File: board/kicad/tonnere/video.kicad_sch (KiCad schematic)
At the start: 38 parts, among them J4 DE15_Pins_HighDensity_Mountin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, J5 HDMI_A, U1 TPD4E02B04DQA, U12 TPD4E02B04DQA, U2 TPD4E02B04DQA, U25 THS7316DR, U3 TPD4E02B04DQA

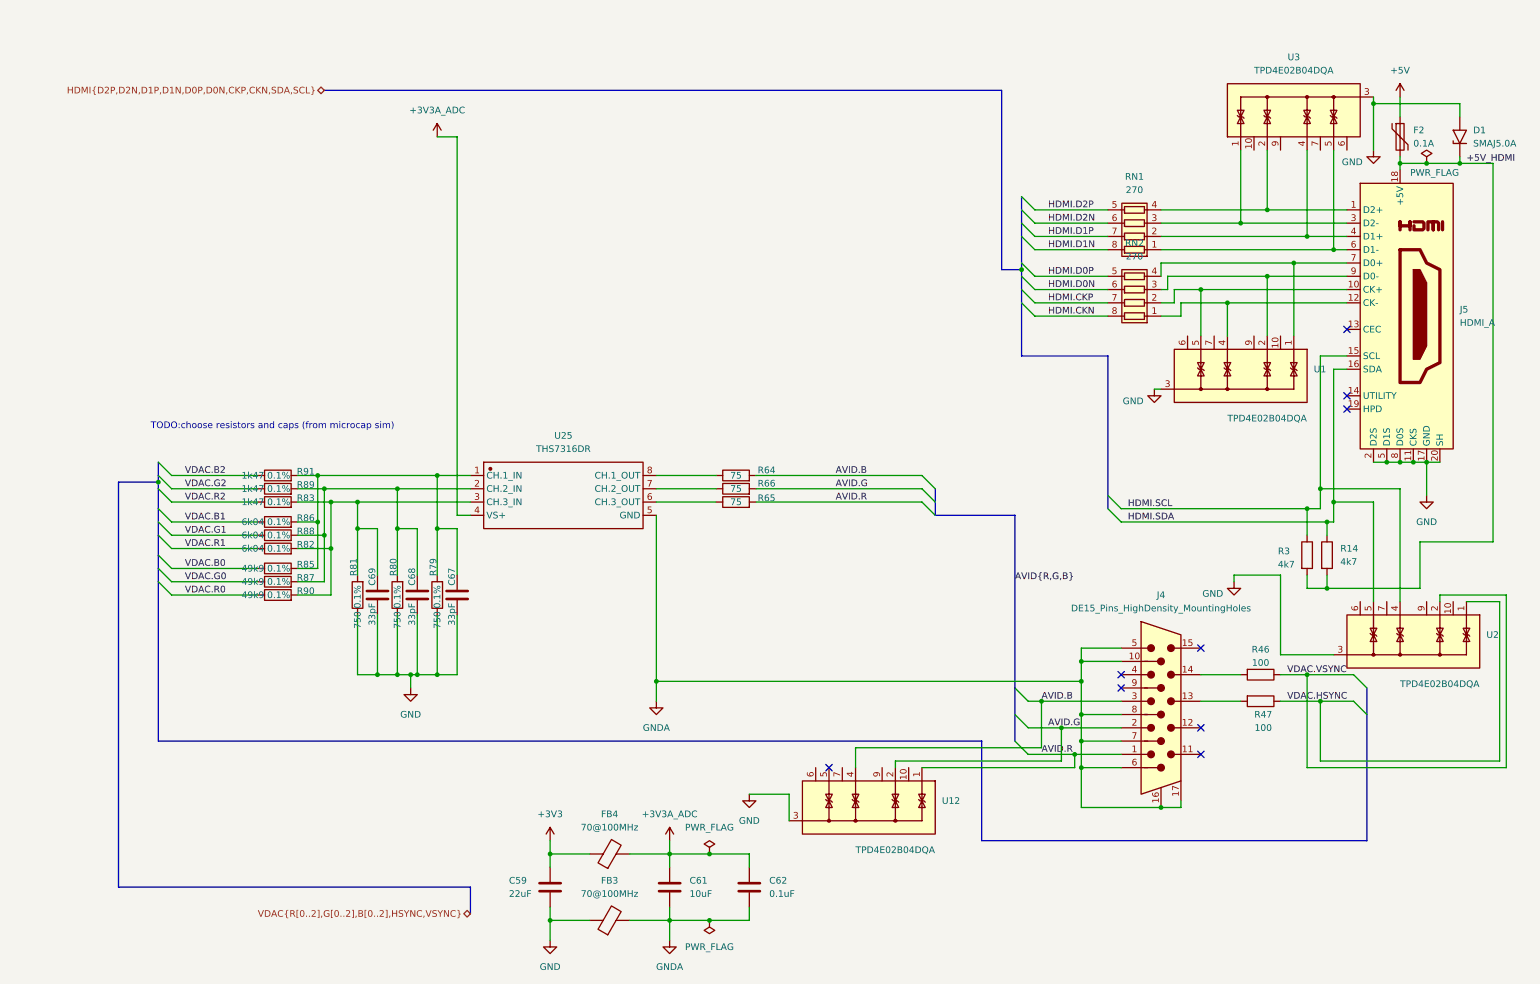
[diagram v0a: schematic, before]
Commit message: Changed video dac to 5 bit R2R and 6th-8th bits as pattern and/or sigma delta.
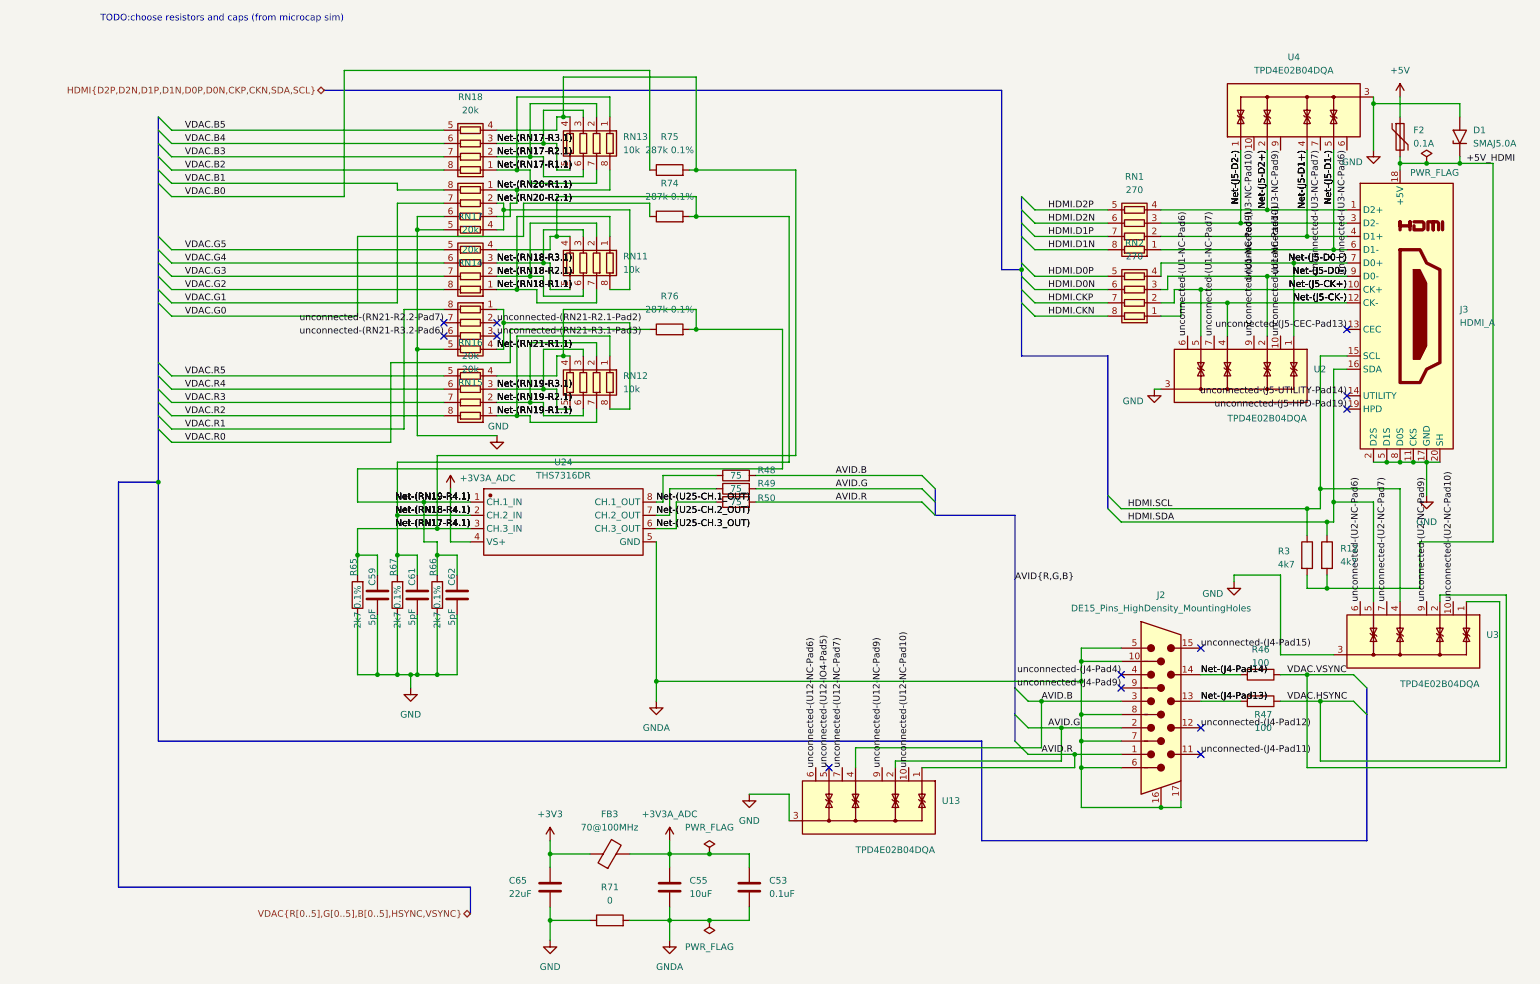
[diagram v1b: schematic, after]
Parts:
- removed FB3: 70@100MHz, Inductor_SMD:L_0805_2012Metric, symbol Device:FerriteBead
- removed R82, R86, R88: 6k04 0.1%, Resistor_SMD:R_0603_1608Metric, symbol Device:R
- removed R83, R89, R91: 1k47 0.1%, Resistor_SMD:R_0603_1608Metric, symbol Device:R
- removed R85, R87, R90: 49k9 0.1%, Resistor_SMD:R_0603_1608Metric, symbol Device:R
- added R71: 0, Resistor_SMD:R_0805_2012Metric, symbol Device:R
- added R74, R75, R76: 287k 0.1%, Resistor_SMD:R_0603_1608Metric, symbol Device:R
- added RN11, RN12, RN13: 10k, Resistor_SMD:R_Array_Convex_4x0402, symbol Device:R_Pack04
- added RN14, RN15, RN16, RN17, RN18: 20k, Resistor_SMD:R_Array_Convex_4x0402, symbol Device:R_Pack04
- C59: renamed from C69; value 33pF -> 5pF; LCSC C1663 -> C282071
- C61: renamed from C68; value 33pF -> 5pF; LCSC C1663 -> C282071
- C62: renamed from C67; value 33pF -> 5pF; LCSC C1663 -> C282071
- R65: renamed from R81; value 750 0.1% -> 2k7 0.1%; LCSC C543637 -> C705760
- R66: renamed from R79; value 750 0.1% -> 2k7 0.1%; LCSC C543637 -> C705760
- R67: renamed from R80; value 750 0.1% -> 2k7 0.1%; LCSC C543637 -> C705760
- renumbered C62 to C53, C61 to C55, C59 to C65, FB4 to FB3, J4 to J2, J5 to J3, R14 to R12, R64 to R48, R66 to R49, R65 to R50, U12 to U13, U1 to U2, U25 to U24, U2 to U3, U3 to U4
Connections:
- net GND: now also R71.1, RN14.5 (R4.2), RN14.6 (R3.2), RN15.5 (R4.2)
- net GNDA: now also R71.2
- net VDAC.B0: now also R75.1
- net VDAC.B1: now also RN14.8 (R1.2)
- net VDAC.B2: now also RN18.8 (R1.2)
- net VDAC.G0: now also R74.1
- net VDAC.G1: now also RN14.7 (R2.2)
- net VDAC.G2: now also RN17.8 (R1.2)
- net VDAC.R0: now also R76.1
- net VDAC.R1: now also RN15.8 (R1.2)
- net VDAC.R2: now also RN16.8 (R1.2)
- net Net-(RN18-R4.1): now reaches C61.1, R67.2, U24.2 (CH.2_IN)
- net Net-(RN18-R4.1): now also R74.2, RN11.4 (R4.1), RN17.4 (R4.1)
- net unconnected-(U2-NC-Pad10): now reaches U3.10 (NC)
- net unconnected-(U2-NC-Pad6): now reaches U3.6 (NC)
- net unconnected-(U2-NC-Pad7): now reaches U3.7 (NC)
- net unconnected-(U2-NC-Pad9): now reaches U3.9 (NC)
- net Net-(RN17-R4.1): now reaches C59.1, R65.2, U24.3 (CH.3_IN)
- net Net-(RN17-R4.1): now also R75.2, RN13.4 (R4.1), RN18.4 (R4.1)
- net Net-(U25-CH.1_OUT): now reaches R48.1, U24.8 (CH.1_OUT)
- net Net-(RN19-R4.1): now reaches C62.1, R66.2, U24.1 (CH.1_IN)
- net Net-(RN19-R4.1): now also R76.2, RN12.4 (R4.1), RN16.4 (R4.1)
- net Net-(J5-D2-): now reaches J3.3 (D2-), RN1.3 (R3.1), U4.1 (IO1)
- net unconnected-(U3-NC-Pad10): now reaches U4.10 (NC)
- net Net-(J5-D2+): now reaches J3.1 (D2+), RN1.4 (R4.1), U4.2 (IO2)
- net Net-(J5-D1+): now reaches J3.4 (D1+), RN1.2 (R2.1), U4.4 (IO3)
- net Net-(J5-D1-): now reaches J3.6 (D1-), RN1.1 (R1.1), U4.5 (IO4)
- net unconnected-(U3-NC-Pad6): now reaches U4.6 (NC)
- net unconnected-(U3-NC-Pad7): now reaches U4.7 (NC)
- net unconnected-(U3-NC-Pad9): now reaches U4.9 (NC)
- net unconnected-(J4-Pad11): now reaches J2.11
- net unconnected-(J4-Pad12): now reaches J2.12
- net Net-(J4-Pad13): now reaches J2.13, R47.2
- net Net-(J4-Pad14): now reaches J2.14, R46.2
- net unconnected-(J4-Pad15): now reaches J2.15
- net unconnected-(J4-Pad4): now reaches J2.4
- net unconnected-(J4-Pad9): now reaches J2.9
- net Net-(U25-CH.3_OUT): now reaches R50.1, U24.6 (CH.3_OUT)
- net Net-(U25-CH.2_OUT): now reaches R49.1, U24.7 (CH.2_OUT)
- net Net-(J5-CK+): now reaches J3.10 (CK+), RN2.2 (R2.1), U2.5 (IO4)
- net Net-(J5-CK-): now reaches J3.12 (CK-), RN2.1 (R1.1), U2.4 (IO3)
- net unconnected-(J5-CEC-Pad13): now reaches J3.13 (CEC)
- net unconnected-(J5-UTILITY-Pad14): now reaches J3.14 (UTILITY)
- net unconnected-(J5-HPD-Pad19): now reaches J3.19 (HPD)
- net Net-(J5-D0+): now reaches J3.7 (D0+), RN2.4 (R4.1), U2.1 (IO1)
- net Net-(J5-D0-): now reaches J3.9 (D0-), RN2.3 (R3.1), U2.2 (IO2)
- net unconnected-(U12-NC-Pad10): now reaches U13.10 (NC)
- net unconnected-(U12-IO4-Pad5): now reaches U13.5 (IO4)
- net unconnected-(U12-NC-Pad6): now reaches U13.6 (NC)
- net unconnected-(U12-NC-Pad7): now reaches U13.7 (NC)
- net unconnected-(U12-NC-Pad9): now reaches U13.9 (NC)
- net unconnected-(U1-NC-Pad10): now reaches U2.10 (NC)
- net unconnected-(U1-NC-Pad6): now reaches U2.6 (NC)
- net unconnected-(U1-NC-Pad7): now reaches U2.7 (NC)
- net unconnected-(U1-NC-Pad9): now reaches U2.9 (NC)
- new net Net-(RN17-R1.1): RN13.1 (R1.1), RN13.7 (R2.2), RN18.1 (R1.1)
- new net Net-(RN17-R2.1): RN13.2 (R2.1), RN13.6 (R3.2), RN18.2 (R2.1)
- new net Net-(RN17-R3.1): RN13.3 (R3.1), RN13.5 (R4.2), RN18.3 (R3.1)
- new net Net-(RN18-R1.1): RN11.1 (R1.1), RN11.7 (R2.2), RN17.1 (R1.1)
- new net Net-(RN18-R2.1): RN11.2 (R2.1), RN11.6 (R3.2), RN17.2 (R2.1)
- new net Net-(RN18-R3.1): RN11.3 (R3.1), RN11.5 (R4.2), RN17.3 (R3.1)
- new net Net-(RN19-R1.1): RN12.1 (R1.1), RN12.7 (R2.2), RN16.1 (R1.1)
- new net Net-(RN19-R2.1): RN12.2 (R2.1), RN12.6 (R3.2), RN16.2 (R2.1)
- new net Net-(RN19-R3.1): RN12.3 (R3.1), RN12.5 (R4.2), RN16.3 (R3.1)
- new net Net-(RN20-R1.1): RN13.8 (R1.2), RN14.1 (R1.1), RN14.3 (R3.1)
- new net Net-(RN20-R2.1): RN11.8 (R1.2), RN14.2 (R2.1), RN14.4 (R4.1)
- new net Net-(RN21-R1.1): RN12.8 (R1.2), RN15.1 (R1.1), RN15.4 (R4.1)
- new net VDAC.B3: RN18.7 (R2.2)
- new net VDAC.B4: RN18.6 (R3.2)
- new net VDAC.B5: RN18.5 (R4.2)
- new net VDAC.G3: RN17.7 (R2.2)
- new net VDAC.G4: RN17.6 (R3.2)
- new net VDAC.G5: RN17.5 (R4.2)
- new net VDAC.R3: RN16.7 (R2.2)
- new net VDAC.R4: RN16.6 (R3.2)
- new net VDAC.R5: RN16.5 (R4.2)
- new net unconnected-(RN21-R2.1-Pad2): RN15.2 (R2.1)
- new net unconnected-(RN21-R2.2-Pad7): RN15.7 (R2.2)
- new net unconnected-(RN21-R3.1-Pad3): RN15.3 (R3.1)
- new net unconnected-(RN21-R3.2-Pad6): RN15.6 (R3.2)
- no-connect marks 9 -> 13
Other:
- moved on the sheet: U24

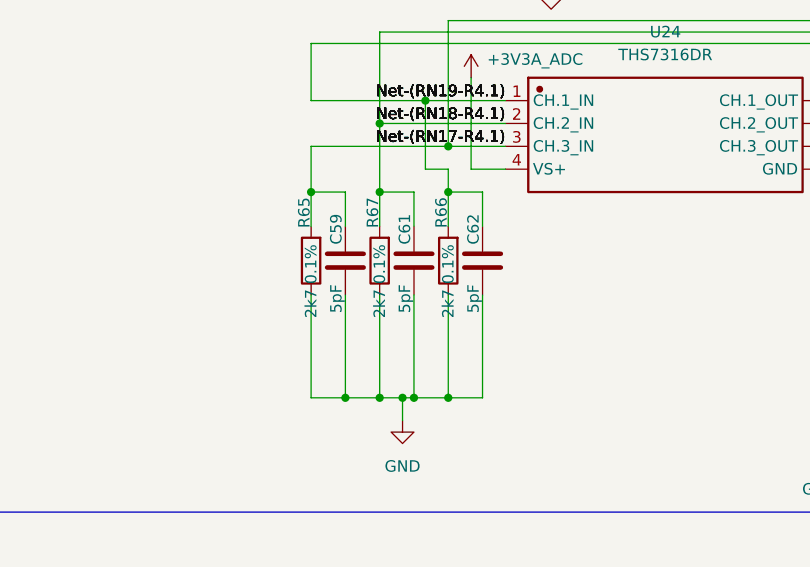
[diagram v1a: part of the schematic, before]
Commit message: After simulation change video dac capacitance from 4.7pF to 1.8pF. Added square for JLCPCB qr code.
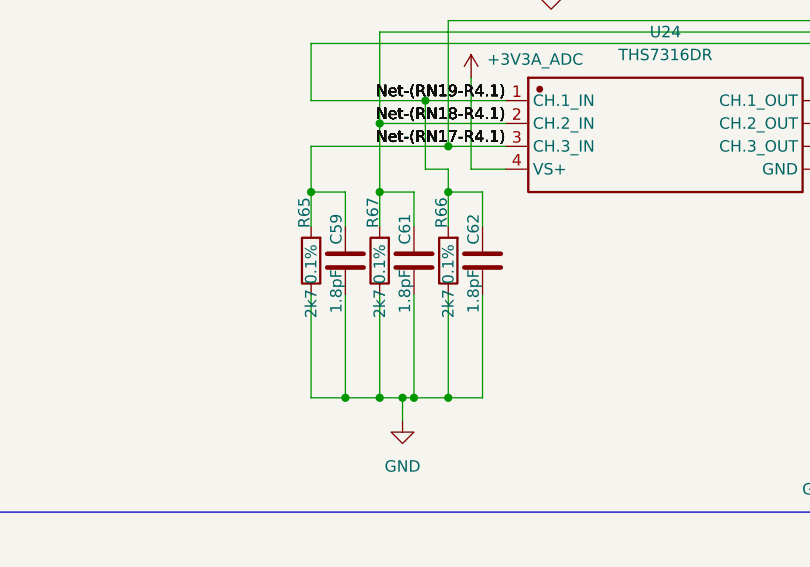
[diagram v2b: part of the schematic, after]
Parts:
- C59, C61, C62: value 5pF -> 1.8pF; LCSC C282071 -> C318660
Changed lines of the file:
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@@
 			)
 		)
-		(property "Value" "5pF"
+		(property "Value" "1.8pF"
 			(at 76.454 120.142 90)
 			(show_name no)
@@
 			)
 		)
-		(property "LCSC" "C282071"
+		(property "LCSC" "C318660"
 			(at 77.47 114.3 0)
 			(hide yes)
@@
 			)
 		)
-		(property "Value" "5pF"
+		(property "Value" "1.8pF"
 			(at 84.074 120.142 90)
 			(show_name no)
@@
 			)
 		)
-		(property "LCSC" "C282071"
+		(property "LCSC" "C318660"
 			(at 85.09 114.3 0)
 			(hide yes)
@@
 			)
 		)
-		(property "Value" "5pF"
+		(property "Value" "1.8pF"
 			(at 68.834 120.142 90)
 			(show_name no)
@@
 			)
 		)
-		(property "LCSC" "C282071"
+		(property "LCSC" "C318660"
 			(at 69.85 114.3 0)
 			(hide yes)
